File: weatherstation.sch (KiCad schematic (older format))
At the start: 29 parts, among them J1 Conn_02x13_Odd_Even, J10 Conn_01x03_Male, J2 Conn_01x02_Male, J3 Conn_01x02_Male, J4 Conn_01x02_Male, J5 Conn_01x02_Male, J6 Conn_01x02_Male, J7 Conn_01x02_Male, J8 Conn_01x02_Male, J9 Conn_01x02_Male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

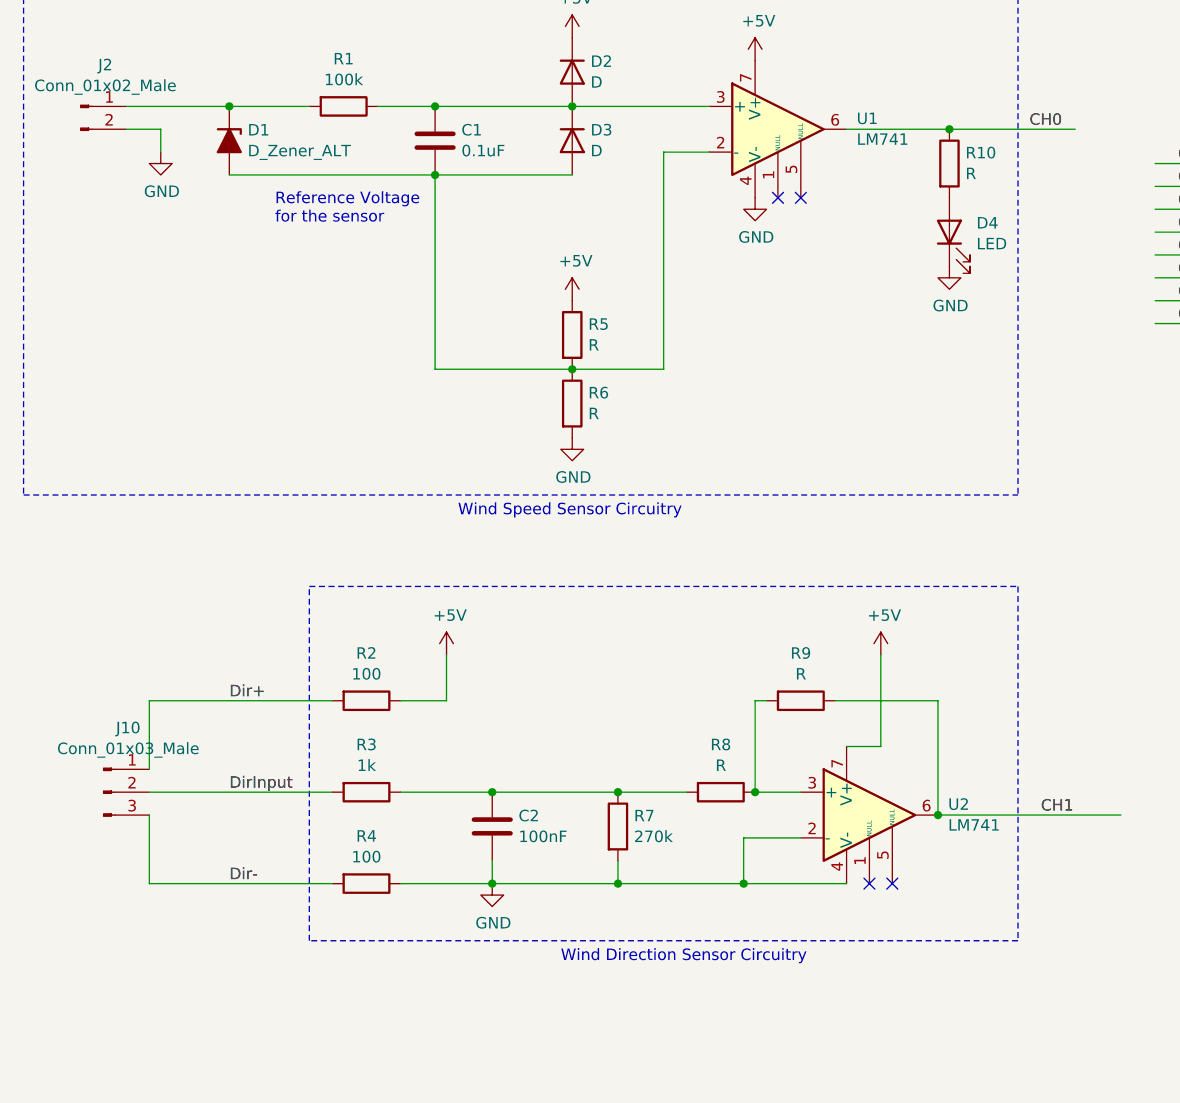
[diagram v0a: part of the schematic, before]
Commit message: Added forgotten component values
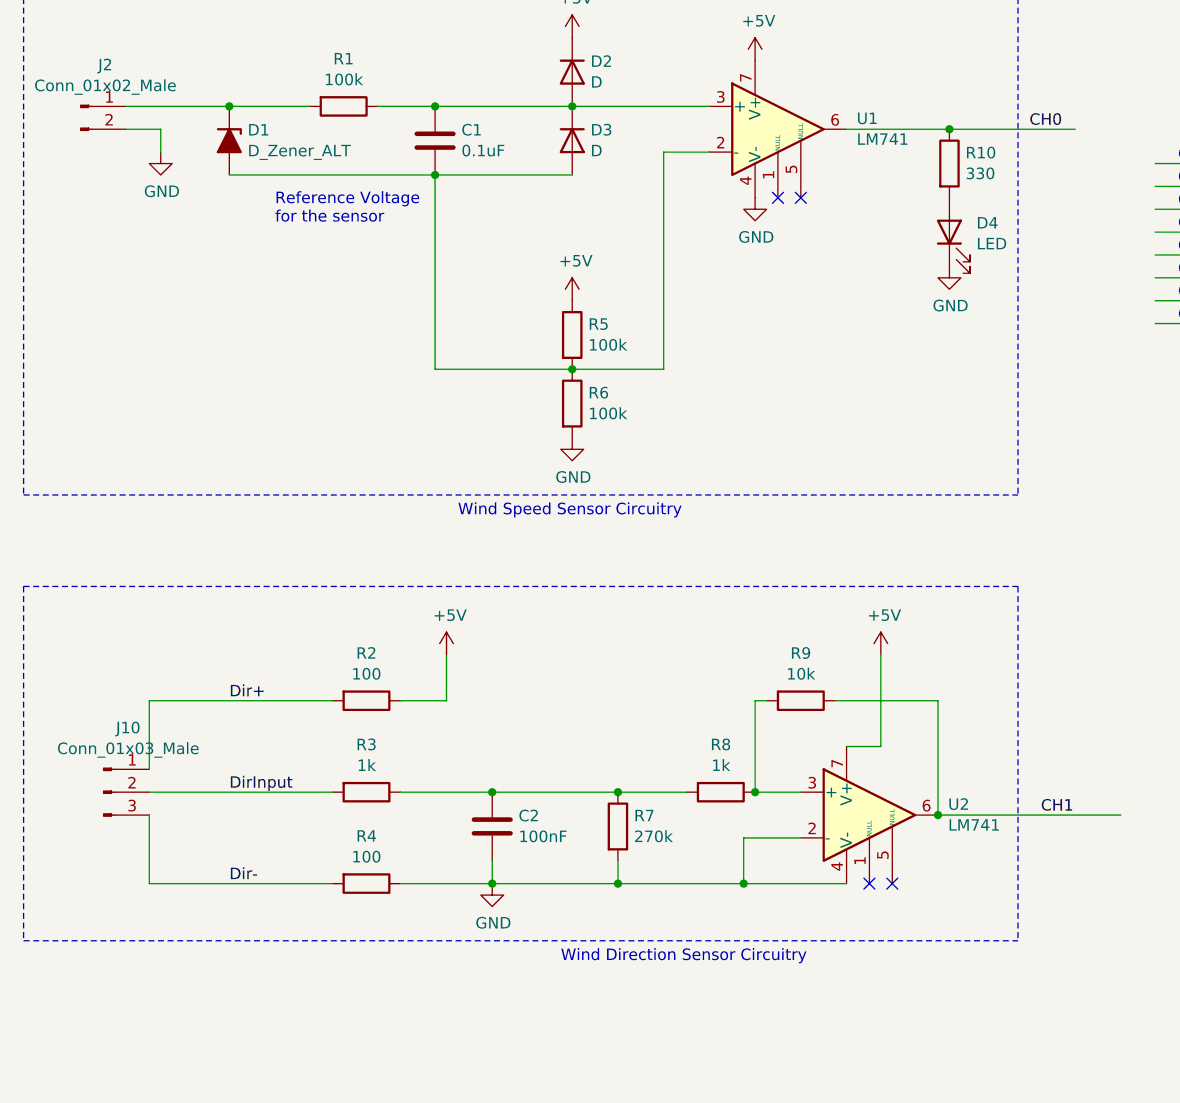
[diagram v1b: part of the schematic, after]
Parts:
- R10: value R -> 330
- R5, R6: value R -> 100k
- R8: value R -> 1k
- R9: value R -> 10k
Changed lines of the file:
@@
 P 3050 2200
 F 0 "R5" H 3120 2246 50  0000 L CNN
-F 1 "R" H 3120 2155 50  0000 L CNN
+F 1 "100k" H 3120 2155 50  0000 L CNN
 F 2 "Resistor_THT:R_Axial_DIN0207_L6.3mm_D2.5mm_P10.16mm_Horizontal" V 2980 2200 50  0001 C CNN
 F 3 "~" H 3050 2200 50  0001 C CNN
@@
 P 3050 2500
 F 0 "R6" H 3120 2546 50  0000 L CNN
-F 1 "R" H 3120 2455 50  0000 L CNN
+F 1 "100k" H 3120 2455 50  0000 L CNN
 F 2 "Resistor_THT:R_Axial_DIN0207_L6.3mm_D2.5mm_P10.16mm_Horizontal" V 2980 2500 50  0001 C CNN
 F 3 "~" H 3050 2500 50  0001 C CNN
@@
 P 4700 1450
 F 0 "R10" H 4770 1496 50  0000 L CNN
-F 1 "R" H 4770 1405 50  0000 L CNN
+F 1 "330" H 4770 1405 50  0000 L CNN
 F 2 "Resistor_THT:R_Axial_DIN0207_L6.3mm_D2.5mm_P10.16mm_Horizontal" V 4630 1450 50  0001 C CNN
 F 3 "~" H 4700 1450 50  0001 C CNN
@@
 Wire Notes Line
 	5000 3300 5000 4850
-Wire Notes Line
-	1900 3300 5000 3300
 Text Label 5100 4300 0    50   ~ 0
 CH1
@@
 P 4050 3800
 F 0 "R9" V 3843 3800 50  0000 C CNN
-F 1 "R" V 3934 3800 50  0000 C CNN
+F 1 "10k" V 3934 3800 50  0000 C CNN
 F 2 "Resistor_THT:R_Axial_DIN0207_L6.3mm_D2.5mm_P10.16mm_Horizontal" V 3980 3800 50  0001 C CNN
 F 3 "~" H 4050 3800 50  0001 C CNN
@@
 P 3700 4200
 F 0 "R8" V 3493 4200 50  0000 C CNN
-F 1 "R" V 3584 4200 50  0000 C CNN
+F 1 "1k" V 3584 4200 50  0000 C CNN
 F 2 "Resistor_THT:R_Axial_DIN0207_L6.3mm_D2.5mm_P10.16mm_Horizontal" V 3630 4200 50  0001 C CNN
 F 3 "~" H 3700 4200 50  0001 C CNN
@@
 Text Label 1550 3800 0    50   ~ 0
 Dir+
-Wire Notes Line
-	5000 4850 1900 4850
-Wire Notes Line
-	1900 4850 1900 3300
 $Comp
 L power:+5V #PWR0113
@@
 	1    0    0    -1
 $EndComp
+Wire Notes Line
+	650  3300 650  4850
+Wire Notes Line
+	650  3300 5000 3300
+Wire Notes Line
+	650  4850 5000 4850
 $EndSCHEMATC
